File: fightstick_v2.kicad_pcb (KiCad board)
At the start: 2 copper layers, 158 parts, among them J1 USB_C_Receptacle_USB2.0, J2 Conn_01x04, J3 Conn_01x03, J9 Conn_01x05, SW1 SW_Push, SW10 SW_Push, SW11 SW_Push, SW12 SW_Push, SW13 SW_Push, SW14 SW_Push, SW15 SW_Push, SW16 SW_Push, SW17 SW_Push, SW19 SW_Push, SW2 SW_Push, SW3 SW_Push, SW4 SW_Push, SW5 SW_Push, SW6 SW_Push, SW7 SW_Push, SW8 SW_Push, SW9 SW_Push, U1 XC6206PxxxMR, U2 W25Q128JVS, U3 RP2040, U4 SRV05-4, U5 74AHCT1G125, Y1 12MHz

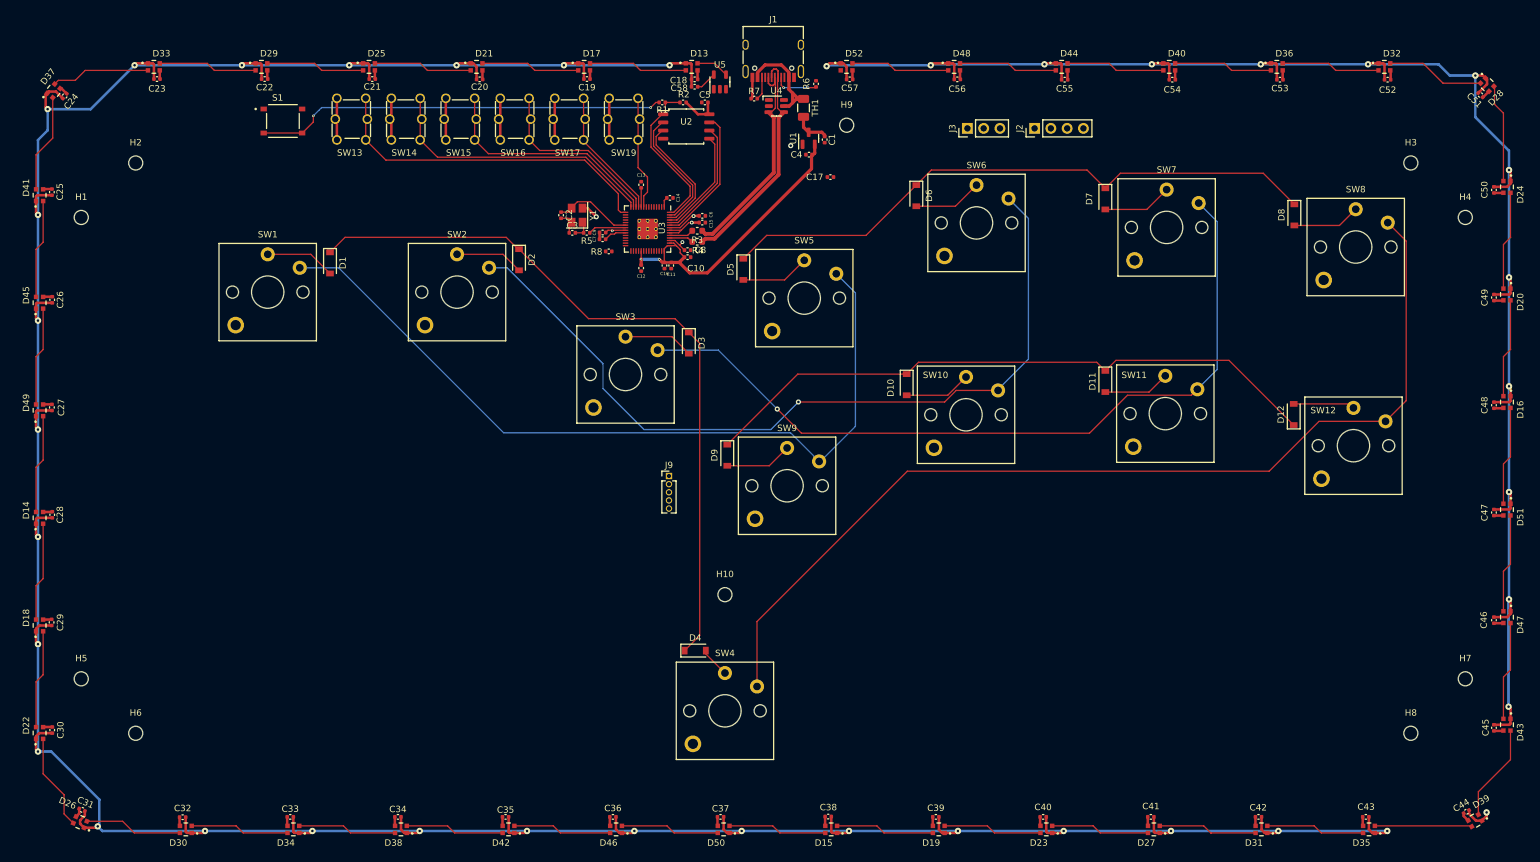
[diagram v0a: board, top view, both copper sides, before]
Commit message: finished routing and mostly clear DRC
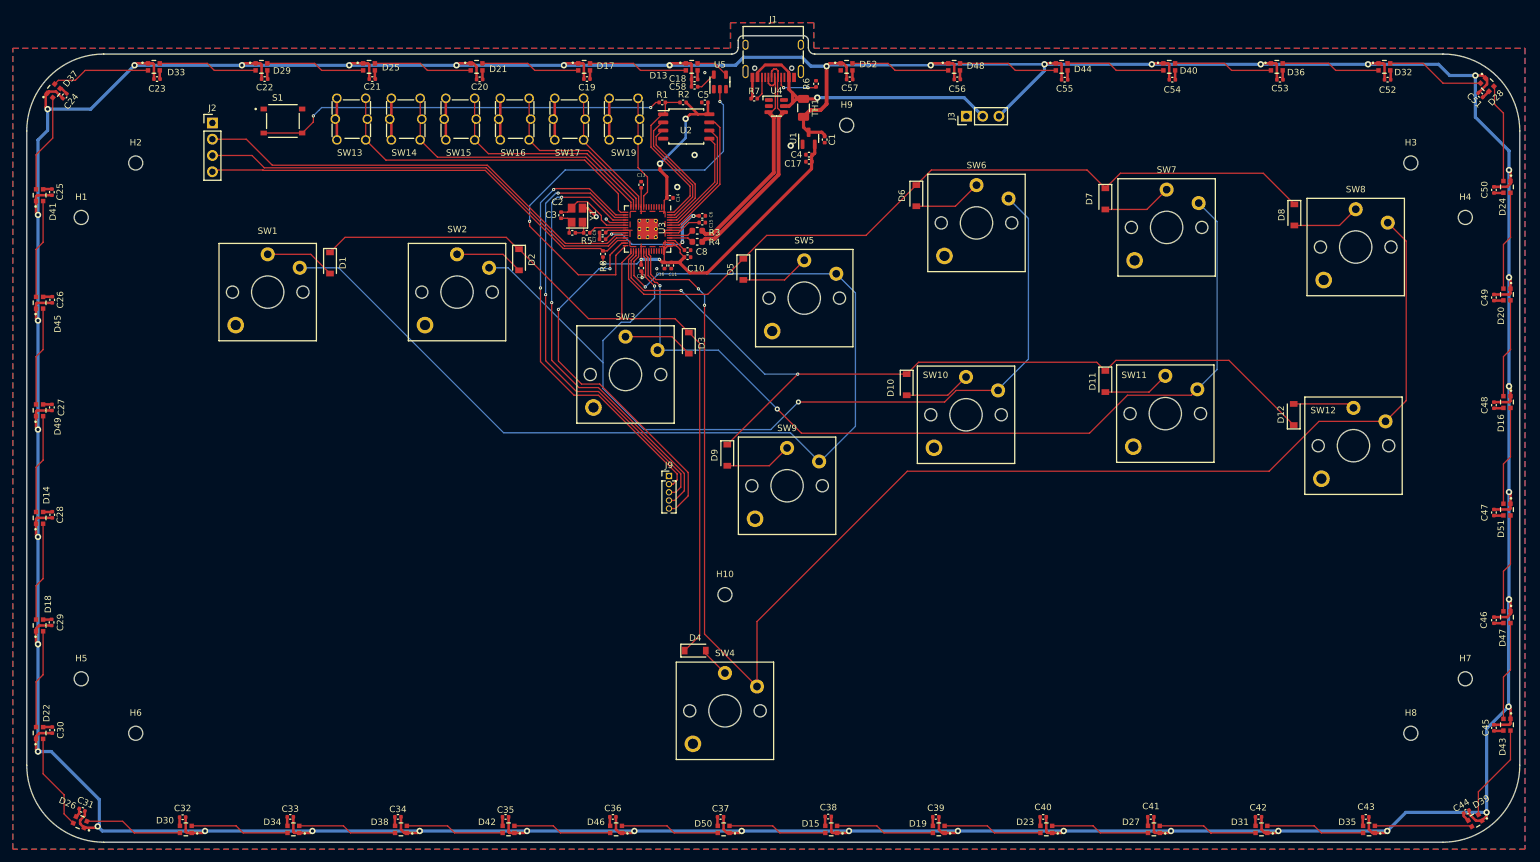
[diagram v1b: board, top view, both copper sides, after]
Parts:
- moved J2 128.3 mm to (75.2, 34.6), turned to 0 degrees
- moved C17 4.12 mm to (168.2, 40.7)
- moved J3 1.91 mm to (192.8, 33.6)
- moved R8 0.98 mm to (136.1, 55.1), turned to 90 degrees
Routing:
- net +5V: track 841.8 -> 923.4 mm
- net COL3: track 154.7 -> 232.7 mm, vias 0 -> 2
- net JOY2: track 0.00 -> 71.9 mm, vias 0 -> 2
- net JOY1: track 0.00 -> 71.8 mm, vias 0 -> 2
- net /SWCLK: track 0.00 -> 71.7 mm
- net JOY3: track 0.00 -> 71.7 mm, vias 0 -> 2
- net /SWD: track 0.00 -> 70.8 mm
- net RESET: track 0.00 -> 70.5 mm
- net D_ARGB_3V3: track 0.00 -> 68.7 mm, vias 0 -> 2
- net JOY4: track 0.00 -> 59.0 mm, vias 0 -> 2
- net COL0: track 126.6 -> 163.9 mm, vias 0 -> 1
- net ROW2: track 99.1 -> 135.9 mm, vias 0 -> 2
- net +3V3: track 71.1 -> 101.7 mm, vias 4 -> 5
- net VBUS: track 17.2 -> 46.4 mm, vias 0 -> 1
- net ROW1: track 95.9 -> 121.8 mm
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- added copper zone on F.Cu, net +3V3
- added copper zone on B.Cu, net GND
- added copper zone on F.Cu, net GND
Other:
- board outline added: 233 x 125.9 mm

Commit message: fixed everything i can tell is wrong
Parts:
- moved C1 1.55 mm to (170.7, 38.8)
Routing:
- net +5V: track 923.4 -> 924.5 mm
- net GND: vias 8 -> 24
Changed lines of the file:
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@@
   )
   (footprint "Capacitor_SMD:C_0402_1005Metric" (layer "F.Cu")
-    (at 170.7 37.25 -90)
+    (at 170.7 38.8 -90)
     (descr "Capacitor SMD 0402 (1005 Metric), square (rectangular) end terminal, IPC_7351 nominal, (Body size source: IPC-SM-782 page 76, https://www.pcb-3d.com/wordpress/wp-content/uploads/ipc-sm-782a_amendment_1_and_2.pdf), generated with kicad-footprint-generator")
     (tags "capacitor")
@@
   (segment (start 83.71707 26.45) (end 83.71707 27.73707) (width 0.4) (layer "F.Cu") (net 2))
   (segment (start 48.742702 78.57) (end 48.728419 78.584283) (width 0.4) (layer "F.Cu") (net 2))
+  (via (at 51 88.5) (size 1) (drill 0.5) (layers "F.Cu" "B.Cu") (free) (net 2))
+  (via (at 246 142.5) (size 1) (drill 0.5) (layers "F.Cu" "B.Cu") (free) (net 2))
+  (via (at 124.69 73.67) (size 1) (drill 0.5) (layers "F.Cu" "B.Cu") (free) (net 2))
+  (via (at 156.17 76.57) (size 1) (drill 0.5) (layers "F.Cu" "B.Cu") (free) (net 2))
   (via (at 135.05 49.3) (size 0.8) (drill 0.4) (layers "F.Cu" "B.Cu") (net 2))
+  (via (at 179 142.5) (size 1) (drill 0.5) (layers "F.Cu" "B.Cu") (free) (net 2))
+  (via (at 129 142.5) (size 1) (drill 0.5) (layers "F.Cu" "B.Cu") (free) (net 2))
   (via (at 150.4 39.65) (size 1) (drill 0.5) (layers "F.Cu" "B.Cu") (free) (net 2))
   (via (at 147.7 44.65) (size 1) (drill 0.5) (layers "F.Cu" "B.Cu") (free) (net 2))
+  (via (at 163.4 107.79) (size 1) (drill 0.5) (layers "F.Cu" "B.Cu") (free) (net 2))
   (via (at 136.6 49.65) (size 0.5) (drill 0.2) (layers "F.Cu" "B.Cu") (net 2))
   (via (at 152 26.8) (size 0.5) (drill 0.2) (layers "F.Cu" "B.Cu") (free) (net 2))
+  (via (at 99.38 47.37) (size 1) (drill 0.5) (layers "F.Cu" "B.Cu") (free) (net 2))
+  (via (at 210.91 65.36) (size 1) (drill 0.5) (layers "F.Cu" "B.Cu") (free) (net 2))
+  (via (at 51 56) (size 1) (drill 0.5) (layers "F.Cu" "B.Cu") (free) (net 2))
+  (via (at 55.5 134) (size 1) (drill 0.5) (layers "F.Cu" "B.Cu") (free) (net 2))
   (via (at 142.2 58.8) (size 0.5) (drill 0.2) (layers "F.Cu" "B.Cu") (free) (net 2))
+  (via (at 241.3 36.79) (size 1) (drill 0.5) (layers "F.Cu" "B.Cu") (free) (net 2))
   (via (at 165.4 38.2) (size 1) (drill 0.5) (layers "F.Cu" "B.Cu") (free) (net 2))
   (via (at 144.5 57.4) (size 0.5) (drill 0.2) (layers "F.Cu" "B.Cu") (free) (net 2))
+  (via (at 242.05 69.58) (size 1) (drill 0.5) (layers "F.Cu" "B.Cu") (free) (net 2))
+  (via (at 217 28.5) (size 1) (drill 0.5) (layers "F.Cu" "B.Cu") (free) (net 2))
+  (via (at 275 104) (size 1) (drill 0.5) (layers "F.Cu" "B.Cu") (free) (net 2))
+  (via (at 274.5 69.5) (size 1) (drill 0.5) (layers "F.Cu" "B.Cu") (free) (net 2))
   (segment (start 135.85 49.11005) (end 135.85 49.8) (width 0.2) (layer "F.Cu") (net 3))
   (segment (start 135.85 49.8) (end 136.649999 50.599999) (width 0.2) (layer "F.Cu") (net 3))
@@
   (segment (start 238.88 142.95) (end 238.88 144.952569) (width 0.4) (layer "F.Cu") (net 26))
   (segment (start 205.28 145.274928) (end 205.455072 145.45) (width 0.4) (layer "F.Cu") (net 26))
+  (segment (start 169.4 36.1) (end 168.2125 36.1) (width 0.5) (layer "F.Cu") (net 26))
   (segment (start 273.415115 27.25) (end 272.25 27.25) (width 0.4) (layer "F.Cu") (net 26))
-  (segment (start 170.7 36.55) (end 170.25 36.1) (width 0.5) (layer "F.Cu") (net 26))
   (segment (start 71.915636 145.45) (end 73.6995 145.45) (width 0.4) (layer "F.Cu") (net 26))
   (segment (start 47.776523 62.73) (end 47.628419 62.878104) (width 0.4) (layer "F.Cu") (net 26))
@@
   (segment (start 221.9 25.35) (end 221.75 25.5) (width 0.4) (layer "F.Cu") (net 26))
   (segment (start 99.62 27.8) (end 99.62 25.546751) (width 0.4) (layer "F.Cu") (net 26))
-  (segment (start 170.7 36.77) (end 170.7 36.55) (width 0.5) (layer "F.Cu") (net 26))
   (segment (start 82.82 25.53293) (end 82.63707 25.35) (width 0.4) (layer "F.Cu") (net 26))
   (segment (start 47.798882 96.28) (end 47.628419 96.450463) (width 0.4) (layer "F.Cu") (net 26))
@@
   (segment (start 272.704717 29.966564) (end 274.071391 28.59989) (width 0.4) (layer "F.Cu") (net 26))
   (segment (start 87.951816 145.45) (end 88.701816 145.45) (width 0.4) (layer "F.Cu") (net 26))
+  (segment (start 170.7 37.4) (end 169.4 36.1) (width 0.5) (layer "F.Cu") (net 26))
   (segment (start 277.728419 94.828054) (end 277.728419 94.078054) (width 0.4) (layer "F.Cu") (net 26))
   (segment (start 167.4 33.7) (end 168.45 32.65) (width 0.6) (layer "F.Cu") (net 26))
@@
   (segment (start 167.4 33.7) (end 167.4 35.3125) (width 0.5) (layer "F.Cu") (net 26))
   (segment (start 207.525 25.35) (end 206.775 25.35) (width 0.4) (layer "F.Cu") (net 26))
-  (segment (start 168.2125 36.1) (end 168.2 36.1125) (width 0.5) (layer "F.Cu") (net 26))
   (segment (start 49.625592 29.756112) (end 49.376742 30.004962) (width 0.4) (layer "F.Cu") (net 26))
   (segment (start 171.45 25.35) (end 173.202641 25.35) (width 0.4) (layer "F.Cu") (net 26))
@@
   (segment (start 190.92 27.85) (end 190.92 25.53118) (width 0.4) (layer "F.Cu") (net 26))
   (segment (start 171.73 145.297287) (end 171.882713 145.45) (width 0.4) (layer "F.Cu") (net 26))
+  (segment (start 170.7 38.32) (end 170.7 37.4) (width 0.5) (layer "F.Cu") (net 26))
   (segment (start 121.38 142.95) (end 121.38 145.305825) (width 0.4) (layer "F.Cu") (net 26))
   (segment (start 47.628419 82.1995) (end 47.928919 82.5) (width 0.4) (layer "F.Cu") (net 26))
@@
   (segment (start 189.98882 25.35) (end 187.5505 25.35) (width 0.4) (layer "F.Cu") (net 26))
   (segment (start 275.15 44.62) (end 277.227934 44.62) (width 0.4) (layer "F.Cu") (net 26))
-  (segment (start 170.25 36.1) (end 168.2125 36.1) (width 0.5) (layer "F.Cu") (net 26))
   (segment (start 223.561179 25.35) (end 221.9 25.35) (width 0.4) (layer "F.Cu") (net 26))
   (segment (start 206.775 25.35) (end 205.15 25.35) (width 0.4) (layer "F.Cu") (net 26))
@@
   (segment (start 57.036944 144.643797) (end 57.25 144.430741) (width 0.4) (layer "F.Cu") (net 26))
   (segment (start 104.58 144.942005) (end 105.087995 145.45) (width 0.4) (layer "F.Cu") (net 26))
+  (segment (start 168.2125 36.1) (end 168.2 36.1125) (width 0.5) (layer "F.Cu") (net 26))
   (segment (start 55.241842 142.736523) (end 54.5 143.478365) (width 0.4) (layer "F.Cu") (net 26))
   (segment (start 47.628419 62.878104) (end 47.628419 63.628104) (width 0.4) (layer "F.Cu") (net 26))
@@
     )
   )
-  (zone (net 2) (net_name "GND") (layer "B.Cu") (name "3v3") (hatch edge 0.508)
+  (zone (net 2) (net_name "GND") (layer "B.Cu") (name "gnd") (hatch edge 0.508)
     (priority 1)
-    (connect_pads yes (clearance 0.15))
-    (min_thickness 0.15) (filled_areas_thickness no)
-    (fill yes (thermal_gap 0.508) (thermal_bridge_width 0.508) (smoothing fillet) (radius 0.2))
+    (connect_pads (clearance 0.3))
+    (min_thickness 0.2) (filled_areas_thickness no)
+    (fill yes (thermal_gap 0.3) (thermal_bridge_width 0.4) (smoothing fillet) (radius 0.2))
     (polygon
       (pts

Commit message: about to try to reroute things
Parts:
- C17: footprint Capacitor_SMD:C_0402_1005Metric -> Capacitor_SMD:C_0805_2012Metric
- moved C4 2.37 mm to (167.9, 42.0)
- moved C17 0.60 mm to (168.2, 40.1)

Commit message: v0.1, shipping this
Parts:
- added G***: LOGO, LOGO, F.Cu at (99.3, 80.5)
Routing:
- net +1V1: track 29.5 -> 23.6 mm
- net COL0: vias 1 -> 2
- net GND: vias 24 -> 28
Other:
- board text added: "JLCJLCJLCJLC"
